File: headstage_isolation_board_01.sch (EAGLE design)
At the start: 49 parts

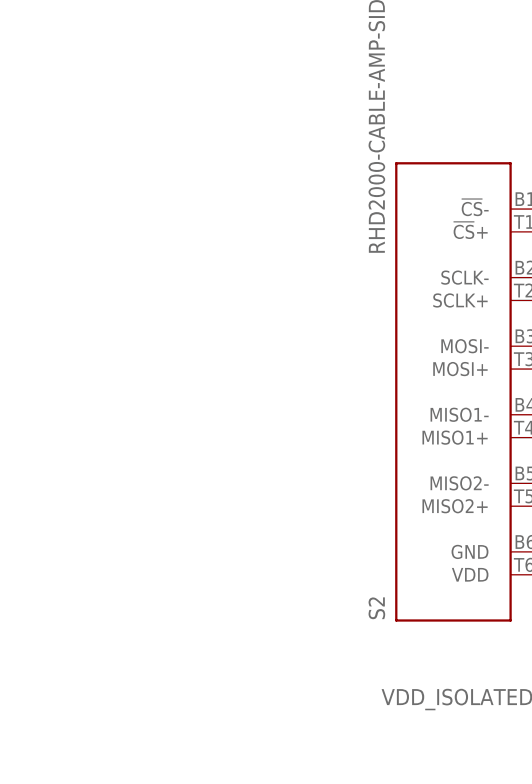
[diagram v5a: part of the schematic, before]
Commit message: added correct connector
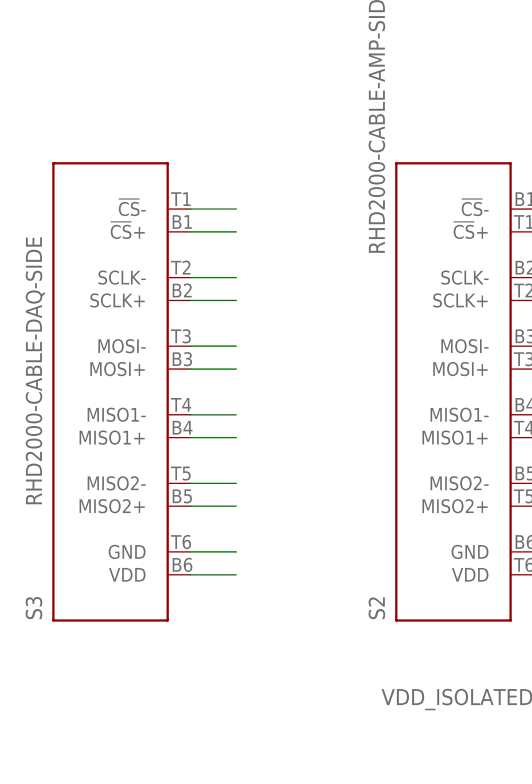
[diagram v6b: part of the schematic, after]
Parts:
- added S3: RHD2000-CABLE-DAQ-SIDE, RHD2000_eval_board:RHD2000-CABLE-DAQ-SIDE
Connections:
- net N$10 renamed MISO2-_ISOLATED
- net N$11 renamed MISO1+_ISOLATED
- net N$12 renamed MISO1-V
- net N$13 renamed MISO2+_ISOLATED
- net N$20 renamed CS-_ISOLATED
- net N$21 renamed SCLK-_ISOLATED
- net N$22 renamed SCLK+_ISOLATED
- net N$23 renamed MOSI-_ISOLATED
- net N$24 renamed MOSI+_ISOLATED
- net N$9 renamed CS+_ISOLATED
- new net CCS+: S3.!CS!+
- new net CCS-: S3.!CS!-
- new net CGND: S3.GND
- new net CMISO1+: S3.MISO1+
- new net CMISO1-: S3.MISO1-
- new net CMISO2+: S3.MISO2+
- new net CMISO2-: S3.MISO2-
- new net CMOSI+: S3.MOSI+
- new net CMOSI-: S3.MOSI-
- new net CSCLK+: S3.SCLK+
- new net CSCLK-: S3.SCLK-
- new net CVDD: S3.VDD
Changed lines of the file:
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@@
 <part name="C17" library="RHD2000_eval_board" deviceset="C" device="_0603" value="100n"/>
 <part name="C18" library="RHD2000_eval_board" deviceset="C" device="_0603" value="100n"/>
+<part name="S3" library="RHD2000_eval_board" deviceset="RHD2000-CABLE-DAQ-SIDE" device=""/>
 </parts>
 <sheets>
@@
 <instance part="C17" gate="C" x="78.74" y="-93.98"/>
 <instance part="C18" gate="C" x="99.06" y="-38.1" rot="R90"/>
+<instance part="S3" gate="A" x="-93.98" y="-63.5" rot="R270"/>
 </instances>
 <busses>
@@
 </segment>
 </net>
-<net name="N$10" class="0">
+<net name="MISO2-_ISOLATED" class="0">
 <segment>
 <pinref part="S2" gate="A" pin="MISO2-"/>
@@
 </segment>
 </net>
-<net name="N$11" class="0">
+<net name="MISO1+_ISOLATED" class="0">
 <segment>
 <pinref part="U$6" gate="G$1" pin="RIN2+"/>
@@
 </segment>
 </net>
-<net name="N$12" class="0">
+<net name="MISO1-V" class="0">
 <segment>
 <pinref part="U$6" gate="G$1" pin="RIN2-"/>
@@
 </segment>
 </net>
-<net name="N$13" class="0">
+<net name="MISO2+_ISOLATED" class="0">
 <segment>
 <pinref part="S2" gate="A" pin="MISO2+"/>
@@
 </segment>
 </net>
-<net name="N$9" class="0">
+<net name="CS+_ISOLATED" class="0">
 <segment>
 <pinref part="S2" gate="A" pin="!CS!+"/>
@@
 </segment>
 </net>
-<net name="N$20" class="0">
+<net name="CS-_ISOLATED" class="0">
 <segment>
 <pinref part="S2" gate="A" pin="!CS!-"/>
@@
 </segment>
 </net>
-<net name="N$21" class="0">
+<net name="SCLK-_ISOLATED" class="0">
 <segment>
 <pinref part="S2" gate="A" pin="SCLK-"/>
@@
 </segment>
 </net>
-<net name="N$22" class="0">
+<net name="SCLK+_ISOLATED" class="0">
 <segment>
 <pinref part="U$5" gate="G$1" pin="DOUT2+"/>
@@
 </segment>
 </net>
-<net name="N$23" class="0">
+<net name="MOSI-_ISOLATED" class="0">
 <segment>
 <pinref part="U$5" gate="G$1" pin="DOUT1-"/>
@@
 </segment>
 </net>
-<net name="N$24" class="0">
+<net name="MOSI+_ISOLATED" class="0">
 <segment>
 <pinref part="U$5" gate="G$1" pin="DOUT1+"/>
@@
 </segment>
 </net>
+<net name="CCS-" class="0">
+<segment>
+<pinref part="S3" gate="A" pin="!CS!-"/>
+<wire x1="-86.36" y1="-43.18" x2="-81.28" y2="-43.18" width="0.1524" layer="91"/>
+</segment>
+</net>
+<net name="CCS+" class="0">
+<segment>
+<pinref part="S3" gate="A" pin="!CS!+"/>
+<wire x1="-86.36" y1="-45.72" x2="-81.28" y2="-45.72" width="0.1524" layer="91"/>
+</segment>
+</net>
+<net name="CSCLK-" class="0">
+<segment>
+<pinref part="S3" gate="A" pin="SCLK-"/>
+<wire x1="-86.36" y1="-50.8" x2="-81.28" y2="-50.8" width="0.1524" layer="91"/>
+</segment>
+</net>
+<net name="CSCLK+" class="0">
+<segment>
+<pinref part="S3" gate="A" pin="SCLK+"/>
+<wire x1="-86.36" y1="-53.34" x2="-81.28" y2="-53.34" width="0.1524" layer="91"/>
+</segment>
+</net>
+<net name="CMOSI-" class="0">
+<segment>
+<pinref part="S3" gate="A" pin="MOSI-"/>
+<wire x1="-86.36" y1="-58.42" x2="-81.28" y2="-58.42" width="0.1524" layer="91"/>
+</segment>
+</net>
+<net name="CMOSI+" class="0">
+<segment>
+<pinref part="S3" gate="A" pin="MOSI+"/>
+<wire x1="-86.36" y1="-60.96" x2="-81.28" y2="-60.96" width="0.1524" layer="91"/>
+</segment>
+</net>
+<net name="CMISO1-" class="0">
+<segment>
+<pinref part="S3" gate="A" pin="MISO1-"/>
+<wire x1="-86.36" y1="-66.04" x2="-81.28" y2="-66.04" width="0.1524" layer="91"/>
+</segment>
+</net>
+<net name="CMISO1+" class="0">
+<segment>
+<pinref part="S3" gate="A" pin="MISO1+"/>
+<wire x1="-86.36" y1="-68.58" x2="-81.28" y2="-68.58" width="0.1524" layer="91"/>
+</segment>
+</net>
+<net name="CMISO2-" class="0">
+<segment>
+<pinref part="S3" gate="A" pin="MISO2-"/>
+<wire x1="-86.36" y1="-73.66" x2="-81.28" y2="-73.66" width="0.1524" layer="91"/>
+</segment>
+</net>
+<net name="CMISO2+" class="0">
+<segment>
+<pinref part="S3" gate="A" pin="MISO2+"/>
+<wire x1="-86.36" y1="-76.2" x2="-81.28" y2="-76.2" width="0.1524" layer="91"/>
+</segment>
+</net>
+<net name="CGND" class="0">
+<segment>
+<pinref part="S3" gate="A" pin="GND"/>
+<wire x1="-86.36" y1="-81.28" x2="-81.28" y2="-81.28" width="0.1524" layer="91"/>
+</segment>
+</net>
+<net name="CVDD" class="0">
+<segment>
+<pinref part="S3" gate="A" pin="VDD"/>
+<wire x1="-86.36" y1="-83.82" x2="-81.28" y2="-83.82" width="0.1524" layer="91"/>
+</segment>
+</net>

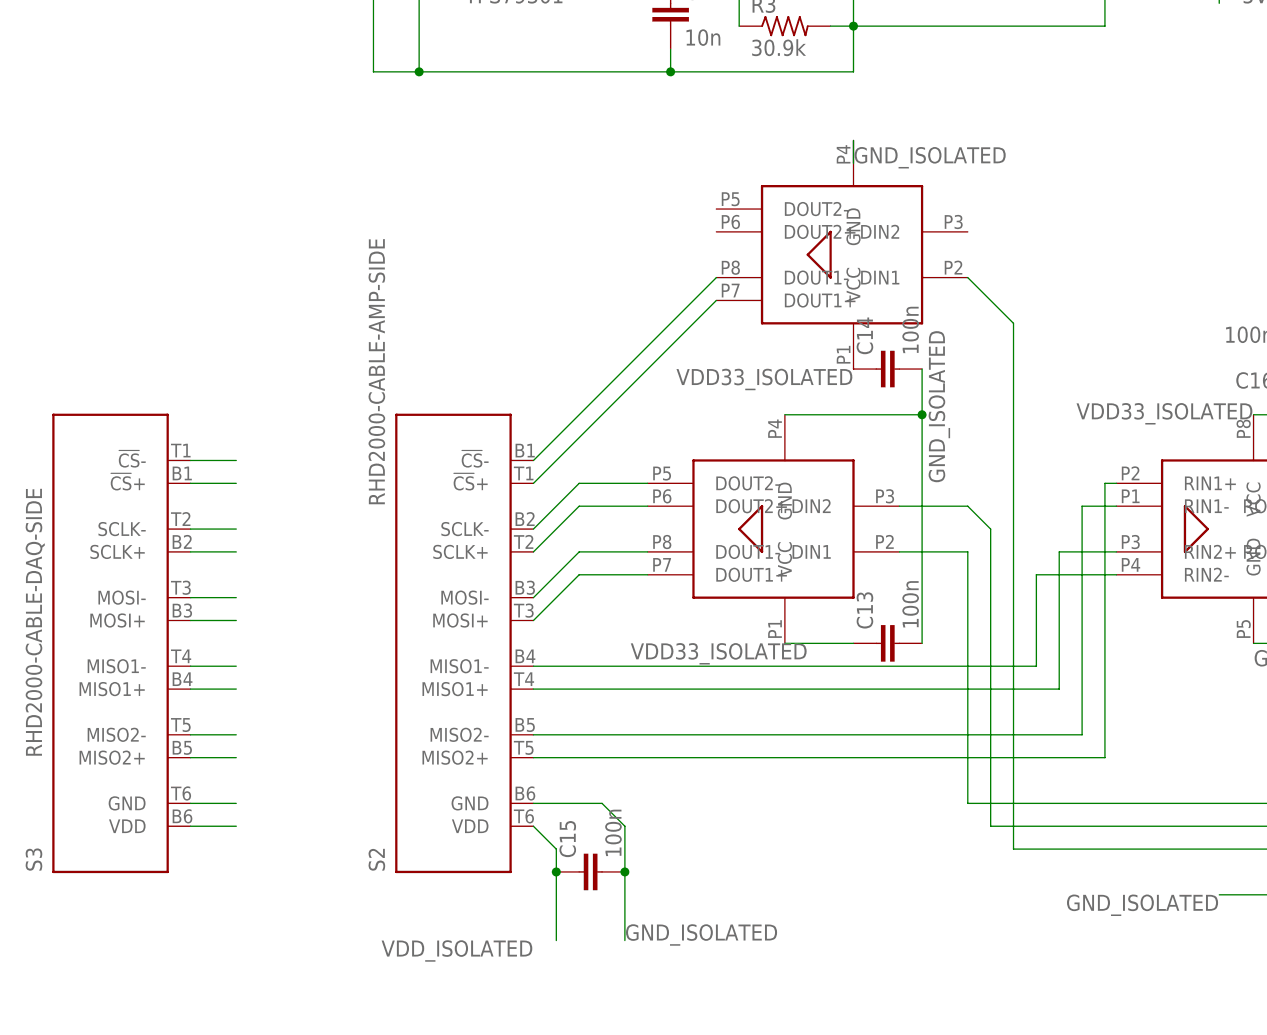
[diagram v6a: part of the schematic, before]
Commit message: routed correct headstage connector
and some other fixes.
Still lacking testpoints
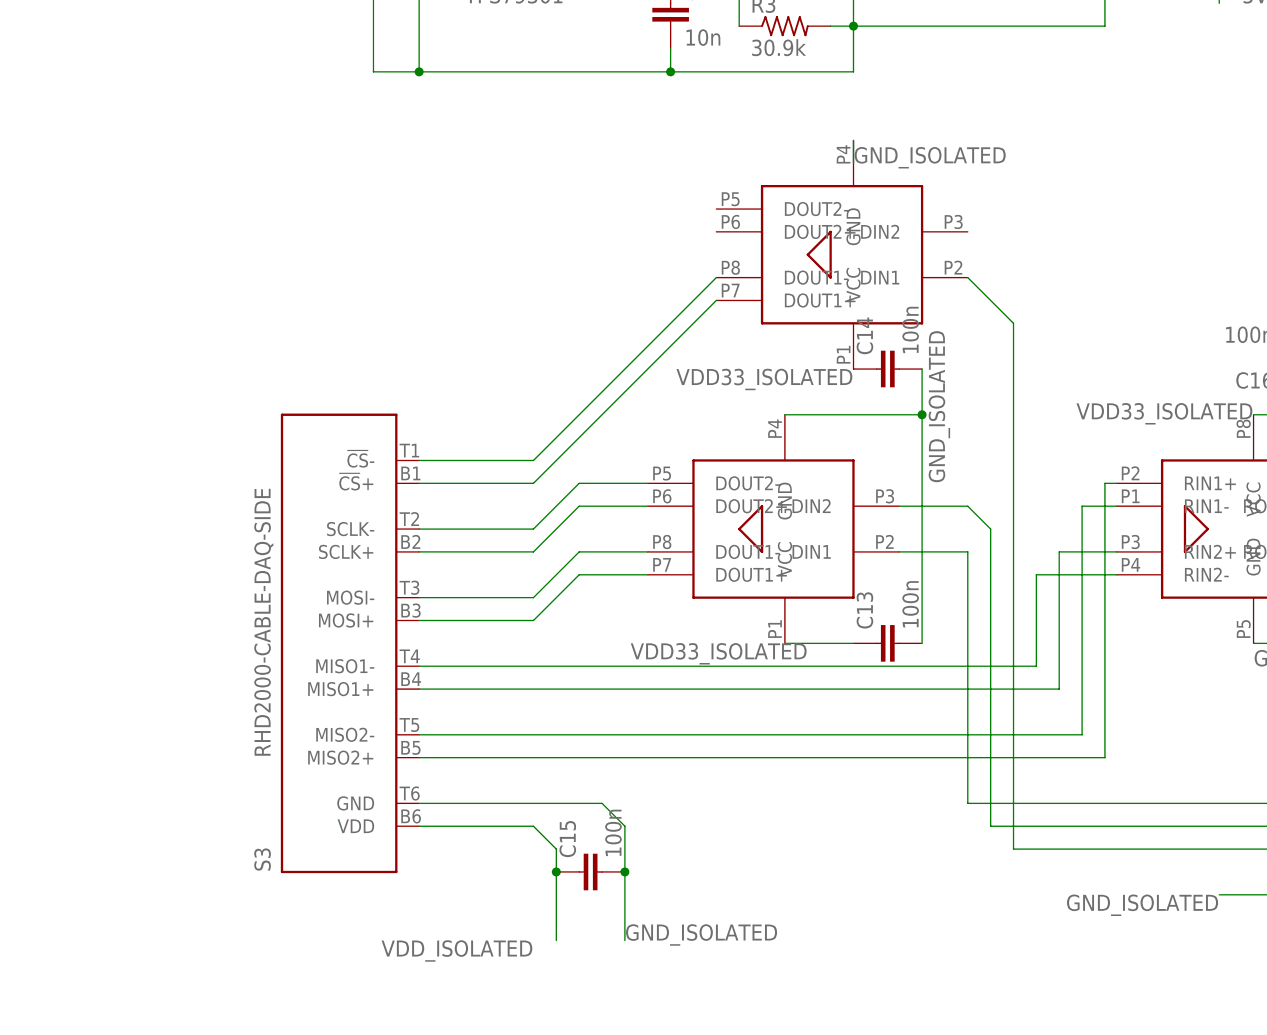
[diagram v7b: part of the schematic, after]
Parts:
- removed S2: RHD2000-CABLE-AMP-SIDE, RHD2000:RHD2000-CABLE-AMP-SIDE
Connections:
- removed net CCS+: S3.!CS!+
- removed net CCS-: S3.!CS!-
- removed net CGND: S3.GND
- removed net CMISO1+: S3.MISO1+
- removed net CMISO1-: S3.MISO1-
- removed net CMISO2+: S3.MISO2+
- removed net CMISO2-: S3.MISO2-
- removed net CMOSI+: S3.MOSI+
- removed net CMOSI-: S3.MOSI-
- removed net CSCLK+: S3.SCLK+
- removed net CSCLK-: S3.SCLK-
- removed net CVDD: S3.VDD
- removed net MISO1-V: S2.MISO1-, U$6.RIN2-
- new net MISO1-_ISOLATED: S3.MISO1-, U$6.RIN2-
- net CS+_ISOLATED: now also S3.!CS!+; no longer S2.!CS!+
- net CS-_ISOLATED: now also S3.!CS!-; no longer S2.!CS!-
- net GND_ISOLATED: now also S3.GND; no longer S2.GND
- net MISO1+_ISOLATED: now also S3.MISO1+; no longer S2.MISO1+
- net MISO2+_ISOLATED: now also S3.MISO2+; no longer S2.MISO2+
- net MISO2-_ISOLATED: now also S3.MISO2-; no longer S2.MISO2-
- net MOSI+_ISOLATED: now also S3.MOSI+; no longer S2.MOSI+
- net MOSI-_ISOLATED: now also S3.MOSI-; no longer S2.MOSI-
- net SCLK+_ISOLATED: now also S3.SCLK+; no longer S2.SCLK+
- net SCLK-_ISOLATED: now also S3.SCLK-; no longer S2.SCLK-
- net VDD_ISOLATED: now also S3.VDD; no longer S2.VDD
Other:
- moved on the sheet: S3
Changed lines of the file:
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@@
 <?xml version="1.0" encoding="utf-8"?>
 <!DOCTYPE eagle SYSTEM "eagle.dtd">
-<eagle version="6.3">
+<eagle version="7.5.0">
 <drawing>
 <settings>
@@
 </classes>
 <parts>
-<part name="S2" library="RHD2000" deviceset="RHD2000-CABLE-AMP-SIDE" device=""/>
 <part name="GND6" library="supply1" deviceset="GND" device=""/>
 <part name="S1" library="RHD2000" deviceset="RHD2000-CABLE-AMP-SIDE" device=""/>
@@
 </plain>
 <instances>
-<instance part="S2" gate="A" x="-55.88" y="-63.5" rot="R270"/>
 <instance part="GND6" gate="1" x="91.44" y="-63.5" rot="R270"/>
 <instance part="S1" gate="A" x="170.18" y="-58.42" rot="R90"/>
@@
 <instance part="C17" gate="C" x="78.74" y="-93.98"/>
 <instance part="C18" gate="C" x="99.06" y="-38.1" rot="R90"/>
-<instance part="S3" gate="A" x="-93.98" y="-63.5" rot="R270"/>
+<instance part="S3" gate="A" x="-68.58" y="-63.5" rot="R270"/>
 </instances>
 <busses>
@@
 <net name="MISO2-_ISOLATED" class="0">
 <segment>
-<pinref part="S2" gate="A" pin="MISO2-"/>
 <pinref part="U$6" gate="G$1" pin="RIN1-"/>
 <wire x1="16.51" y1="-48.26" x2="12.7" y2="-48.26" width="0.1524" layer="91"/>
 <wire x1="12.7" y1="-48.26" x2="12.7" y2="-73.66" width="0.1524" layer="91"/>
-<wire x1="12.7" y1="-73.66" x2="-48.26" y2="-73.66" width="0.1524" layer="91"/>
+<wire x1="12.7" y1="-73.66" x2="-60.96" y2="-73.66" width="0.1524" layer="91"/>
+<pinref part="S3" gate="A" pin="MISO2-"/>
 </segment>
 </net>
@@
 <wire x1="16.51" y1="-53.34" x2="10.16" y2="-53.34" width="0.1524" layer="91"/>
 <wire x1="10.16" y1="-53.34" x2="10.16" y2="-68.58" width="0.1524" layer="91"/>
-<pinref part="S2" gate="A" pin="MISO1+"/>
-<wire x1="10.16" y1="-68.58" x2="-48.26" y2="-68.58" width="0.1524" layer="91"/>
-</segment>
-</net>
-<net name="MISO1-V" class="0">
+<wire x1="10.16" y1="-68.58" x2="-60.96" y2="-68.58" width="0.1524" layer="91"/>
+<pinref part="S3" gate="A" pin="MISO1+"/>
+</segment>
+</net>
+<net name="MISO1-_ISOLATED" class="0">
 <segment>
 <pinref part="U$6" gate="G$1" pin="RIN2-"/>
 <wire x1="7.62" y1="-55.88" x2="16.51" y2="-55.88" width="0.1524" layer="91"/>
 <wire x1="7.62" y1="-55.88" x2="7.62" y2="-66.04" width="0.1524" layer="91"/>
-<pinref part="S2" gate="A" pin="MISO1-"/>
-<wire x1="7.62" y1="-66.04" x2="-48.26" y2="-66.04" width="0.1524" layer="91"/>
+<wire x1="7.62" y1="-66.04" x2="-60.96" y2="-66.04" width="0.1524" layer="91"/>
+<pinref part="S3" gate="A" pin="MISO1-"/>
 </segment>
 </net>
 <net name="MISO2+_ISOLATED" class="0">
 <segment>
-<pinref part="S2" gate="A" pin="MISO2+"/>
-<wire x1="-48.26" y1="-76.2" x2="15.24" y2="-76.2" width="0.1524" layer="91"/>
+<wire x1="-60.96" y1="-76.2" x2="15.24" y2="-76.2" width="0.1524" layer="91"/>
 <wire x1="15.24" y1="-76.2" x2="15.24" y2="-45.72" width="0.1524" layer="91"/>
 <pinref part="U$6" gate="G$1" pin="RIN1+"/>
 <wire x1="15.24" y1="-45.72" x2="16.51" y2="-45.72" width="0.1524" layer="91"/>
+<pinref part="S3" gate="A" pin="MISO2+"/>
 </segment>
 </net>
@@
 </segment>
 </net>
-<net name="CS+_ISOLATED" class="0">
-<segment>
-<pinref part="S2" gate="A" pin="!CS!+"/>
-<wire x1="-27.94" y1="-25.4" x2="-48.26" y2="-45.72" width="0.1524" layer="91"/>
-<pinref part="U$9" gate="G$1" pin="DOUT1+"/>
-</segment>
-</net>
 <net name="CS-_ISOLATED" class="0">
 <segment>
-<pinref part="S2" gate="A" pin="!CS!-"/>
 <wire x1="-27.94" y1="-22.86" x2="-48.26" y2="-43.18" width="0.1524" layer="91"/>
 <pinref part="U$9" gate="G$1" pin="DOUT1-"/>
+<pinref part="S3" gate="A" pin="!CS!-"/>
+<wire x1="-48.26" y1="-43.18" x2="-60.96" y2="-43.18" width="0.1524" layer="91"/>
 </segment>
 </net>
@@
 <net name="SCLK-_ISOLATED" class="0">
 <segment>
-<pinref part="S2" gate="A" pin="SCLK-"/>
 <wire x1="-48.26" y1="-50.8" x2="-43.18" y2="-45.72" width="0.1524" layer="91"/>
 <pinref part="U$5" gate="G$1" pin="DOUT2-"/>
 <wire x1="-43.18" y1="-45.72" x2="-35.56" y2="-45.72" width="0.1524" layer="91"/>
-</segment>
-</net>
-<net name="SCLK+_ISOLATED" class="0">
-<segment>
-<pinref part="U$5" gate="G$1" pin="DOUT2+"/>
-<pinref part="S2" gate="A" pin="SCLK+"/>
-<wire x1="-35.56" y1="-48.26" x2="-43.18" y2="-48.26" width="0.1524" layer="91"/>
-<wire x1="-43.18" y1="-48.26" x2="-48.26" y2="-53.34" width="0.1524" layer="91"/>
+<pinref part="S3" gate="A" pin="SCLK-"/>
+<wire x1="-48.26" y1="-50.8" x2="-60.96" y2="-50.8" width="0.1524" layer="91"/>
 </segment>
 </net>
@@
 <segment>
 <pinref part="U$5" gate="G$1" pin="DOUT1-"/>
-<pinref part="S2" gate="A" pin="MOSI-"/>
 <wire x1="-35.56" y1="-53.34" x2="-43.18" y2="-53.34" width="0.1524" layer="91"/>
 <wire x1="-43.18" y1="-53.34" x2="-48.26" y2="-58.42" width="0.1524" layer="91"/>
+<pinref part="S3" gate="A" pin="MOSI-"/>
+<wire x1="-48.26" y1="-58.42" x2="-60.96" y2="-58.42" width="0.1524" layer="91"/>
 </segment>
 </net>
@@
 <segment>
 <pinref part="U$5" gate="G$1" pin="DOUT1+"/>
-<pinref part="S2" gate="A" pin="MOSI+"/>
 <wire x1="-35.56" y1="-55.88" x2="-43.18" y2="-55.88" width="0.1524" layer="91"/>
 <wire x1="-43.18" y1="-55.88" x2="-48.26" y2="-60.96" width="0.1524" layer="91"/>
+<pinref part="S3" gate="A" pin="MOSI+"/>
+<wire x1="-48.26" y1="-60.96" x2="-60.96" y2="-60.96" width="0.1524" layer="91"/>
 </segment>
 </net>
@@
 <segment>
 <wire x1="-38.1" y1="-83.82" x2="-40.64" y2="-81.28" width="0.1524" layer="91"/>
-<pinref part="S2" gate="A" pin="GND"/>
-<wire x1="-40.64" y1="-81.28" x2="-48.26" y2="-81.28" width="0.1524" layer="91"/>
 <label x="-38.1" y="-96.52" size="1.778" layer="95"/>
 <wire x1="-38.1" y1="-83.82" x2="-38.1" y2="-96.52" width="0.1524" layer="91"/>
+<pinref part="S3" gate="A" pin="GND"/>
+<wire x1="-40.64" y1="-81.28" x2="-60.96" y2="-81.28" width="0.1524" layer="91"/>
 </segment>
 <segment>
@@
 <segment>
 <wire x1="-45.72" y1="-86.36" x2="-45.72" y2="-88.9" width="0.1524" layer="91"/>
-<pinref part="S2" gate="A" pin="VDD"/>
 <wire x1="-45.72" y1="-88.9" x2="-45.72" y2="-96.52" width="0.1524" layer="91"/>
 <wire x1="-45.72" y1="-86.36" x2="-48.26" y2="-83.82" width="0.1524" layer="91"/>
@@
 <pinref part="C15" gate="C" pin="1"/>
 <junction x="-45.72" y="-88.9"/>
+<pinref part="S3" gate="A" pin="VDD"/>
+<wire x1="-48.26" y1="-83.82" x2="-60.96" y2="-83.82" width="0.1524" layer="91"/>
 </segment>
 <segment>
@@
 </segment>
 </net>
-<net name="CCS-" class="0">
-<segment>
-<pinref part="S3" gate="A" pin="!CS!-"/>
-<wire x1="-86.36" y1="-43.18" x2="-81.28" y2="-43.18" width="0.1524" layer="91"/>
-</segment>
-</net>
-<net name="CCS+" class="0">
+<net name="CS+_ISOLATED" class="0">
 <segment>
 <pinref part="S3" gate="A" pin="!CS!+"/>
-<wire x1="-86.36" y1="-45.72" x2="-81.28" y2="-45.72" width="0.1524" layer="91"/>
-</segment>
-</net>
-<net name="CSCLK-" class="0">
-<segment>
-<pinref part="S3" gate="A" pin="SCLK-"/>
-<wire x1="-86.36" y1="-50.8" x2="-81.28" y2="-50.8" width="0.1524" layer="91"/>
-</segment>
-</net>
-<net name="CSCLK+" class="0">
+<wire x1="-27.94" y1="-25.4" x2="-48.26" y2="-45.72" width="0.1524" layer="91"/>
+<pinref part="U$9" gate="G$1" pin="DOUT1+"/>
+<wire x1="-60.96" y1="-45.72" x2="-48.26" y2="-45.72" width="0.1524" layer="91"/>
+</segment>
+</net>
+<net name="SCLK+_ISOLATED" class="0">
 <segment>
 <pinref part="S3" gate="A" pin="SCLK+"/>
-<wire x1="-86.36" y1="-53.34" x2="-81.28" y2="-53.34" width="0.1524" layer="91"/>
-</segment>
-</net>
-<net name="CMOSI-" class="0">
-<segment>
-<pinref part="S3" gate="A" pin="MOSI-"/>
-<wire x1="-86.36" y1="-58.42" x2="-81.28" y2="-58.42" width="0.1524" layer="91"/>
-</segment>
-</net>
-<net name="CMOSI+" class="0">
-<segment>
-<pinref part="S3" gate="A" pin="MOSI+"/>
-<wire x1="-86.36" y1="-60.96" x2="-81.28" y2="-60.96" width="0.1524" layer="91"/>
-</segment>
-</net>
-<net name="CMISO1-" class="0">
-<segment>
-<pinref part="S3" gate="A" pin="MISO1-"/>
-<wire x1="-86.36" y1="-66.04" x2="-81.28" y2="-66.04" width="0.1524" layer="91"/>
-</segment>
-</net>
-<net name="CMISO1+" class="0">
-<segment>
-<pinref part="S3" gate="A" pin="MISO1+"/>
-<wire x1="-86.36" y1="-68.58" x2="-81.28" y2="-68.58" width="0.1524" layer="91"/>
-</segment>
-</net>
-<net name="CMISO2-" class="0">
-<segment>
-<pinref part="S3" gate="A" pin="MISO2-"/>
-<wire x1="-86.36" y1="-73.66" x2="-81.28" y2="-73.66" width="0.1524" layer="91"/>
-</segment>
-</net>
-<net name="CMISO2+" class="0">
-<segment>
-<pinref part="S3" gate="A" pin="MISO2+"/>
-<wire x1="-86.36" y1="-76.2" x2="-81.28" y2="-76.2" width="0.1524" layer="91"/>
-</segment>
-</net>
-<net name="CGND" class="0">
-<segment>
-<pinref part="S3" gate="A" pin="GND"/>
-<wire x1="-86.36" y1="-81.28" x2="-81.28" y2="-81.28" width="0.1524" layer="91"/>
-</segment>
-</net>
-<net name="CVDD" class="0">
-<segment>
-<pinref part="S3" gate="A" pin="VDD"/>
-<wire x1="-86.36" y1="-83.82" x2="-81.28" y2="-83.82" width="0.1524" layer="91"/>
-</segment>
-</net>
+<pinref part="U$5" gate="G$1" pin="DOUT2+"/>
+<wire x1="-35.56" y1="-48.26" x2="-43.18" y2="-48.26" width="0.1524" layer="91"/>
+<wire x1="-43.18" y1="-48.26" x2="-48.26" y2="-53.34" width="0.1524" layer="91"/>
+<wire x1="-60.96" y1="-53.34" x2="-48.26" y2="-53.34" width="0.1524" layer="91"/>
+</segment>
+</net>
